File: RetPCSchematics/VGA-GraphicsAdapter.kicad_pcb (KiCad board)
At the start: 2 copper layers, 183.4 x 101.3 mm, 40 parts, among them J1 Bus_ISA_8bit, J2 74320-9004, U1 74AUC2G125, U10 ATmega644P-20PU, U11 628128, U12 628128, U13 SN74LVC245AN, U14 74LS245, U15 74LVC2G240, U16 74LVC2G240, U17 74LVC1G18, U18 74LVC1G18, U19 74LVC1G18, U2 74LVC2G240, U20 74LVC1G18, U21 ATF22V10D, U22 74LS245, U23 74LVC1G373, U24 74LVC1G373, U25 74LVC1G373, U26 74LVC1G373, U27 74LVC1G373, U28 74LVC1G373, U29 74LVC1G373, U3 ATF22V10D, U30 74LVC1G373, U31 74LVC1G373, U32 74LVC1G373, U33 74LVC1G373, U34 74LVC1G373, U36 TFP410, U37 ATF750C, U4 ATF22V10D, U5 74LS245, U6 ATF22V10D, U7 74LS245, U8 74LS245, U9 74LS245, X1 DGOF5S3

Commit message: EOD sync
Only control signals left to route
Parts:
- moved U2 108.6 mm to (157.1, 71.0), turned to 180 degrees
- moved U29 67.6 mm to (209.3, 76.2)
- moved U25 58.9 mm to (198.6, 56.0)
- moved U28 55.9 mm to (209.3, 72.4)
- moved U30 55.3 mm to (209.4, 64.3)
- moved U26 52.5 mm to (205.6, 48.6)
- moved U31 51.8 mm to (205.6, 57.1)
- moved U33 50.8 mm to (205.6, 52.6)
- moved U34 46.9 mm to (212.2, 52.5)
- moved U27 43.6 mm to (209.3, 68.7)
- moved U32 42.3 mm to (212.2, 48.3)
- moved X1 42.2 mm to (122.9, 57.4)
- moved U6 38.0 mm to (144.7, 57.9)
- moved U15 16.4 mm to (119.3, 106.8)
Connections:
- U2 pad 1: GND -> (no net)
- U2 pad 2: Net-(U2-Pad2) -> (no net)
- U2 pad 6: GEnd -> (no net)
- U4 pad 22: Net-(U2-Pad2) -> GEnd
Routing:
- net LoadEnable: track 0.00 -> 206.7 mm, vias 0 -> 9
- net GClock: track 0.00 -> 121.5 mm, vias 0 -> 5
- net DE: track 0.00 -> 79.4 mm
- net OP: track 0.00 -> 67.7 mm, vias 0 -> 3
- net Net-(U23-Pad4): track 0.00 -> 63.7 mm, vias 0 -> 3
- net Net-(U24-Pad4): track 0.00 -> 62.8 mm, vias 0 -> 2
- net Net-(U26-Pad4): track 0.00 -> 56.0 mm, vias 0 -> 5
- net Net-(U25-Pad4): track 0.00 -> 54.6 mm, vias 0 -> 4
- net Net-(U32-Pad4): track 0.00 -> 50.8 mm, vias 0 -> 2
- net Net-(U34-Pad4): track 0.00 -> 40.5 mm, vias 0 -> 4
- net Net-(U31-Pad4): track 0.00 -> 39.1 mm, vias 0 -> 2
- net Net-(U33-Pad4): track 0.00 -> 39.1 mm, vias 0 -> 1
- net Net-(U28-Pad4): track 0.00 -> 38.5 mm, vias 0 -> 3
- net Net-(U27-Pad4): track 0.00 -> 33.3 mm, vias 0 -> 2
- net Net-(U30-Pad4): track 0.00 -> 31.7 mm, vias 0 -> 2
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
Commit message: EOD sync
end of day sync
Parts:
- added REF**: PinHeader_1x02_P1.00mm_Vertical, Connector_PinHeader_1.00mm:PinHeader_1x02_P1.00mm_Vertical, F.Cu at (219.8, 48.0)
- moved J1 0.68 mm to (184.4, 135.3)
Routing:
- net Net-(U16-Pad3): track 0.00 -> 66.2 mm, vias 0 -> 3
- net GEnd: track 0.00 -> 55.3 mm, vias 0 -> 1
- net Net-(J2-Pad18): track 0.00 -> 28.7 mm, vias 0 -> 1
- net ALEN: track 27.3 -> 53.8 mm, vias 0 -> 3
- net Net-(J2-Pad23): track 0.00 -> 23.3 mm, vias 0 -> 1
- net Net-(J2-Pad17): track 0.00 -> 23.1 mm, vias 0 -> 1
- net GClock: track 121.5 -> 144.4 mm, vias 5 -> 6
- net Net-(J2-Pad24): track 0.00 -> 20.1 mm, vias 0 -> 1
- net Net-(J2-Pad9): track 0.00 -> 15.2 mm, vias 0 -> 1
- net Net-(J2-Pad1): track 0.00 -> 14.0 mm, vias 0 -> 1
- net Net-(J2-Pad2): track 0.00 -> 13.2 mm, vias 0 -> 1
- net /A0: track 1222.7 -> 1225.2 mm, vias 26 -> 28
- added copper zone on F.Cu, net GND
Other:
- board size 183.4 x 101.3 mm -> 136.7 x 101.3 mm

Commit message: sync
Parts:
- removed the REF** at (219.8, 48.0)
- added J3: Conn_01x02_Male, Connector_PinHeader_1.00mm:PinHeader_1x02_P1.00mm_Vertical, F.Cu at (218.2, 47.2)
- added REF**: OSHW-Symbol_6.7x6mm_SilkScreen, Symbol:OSHW-Symbol_6.7x6mm_SilkScreen, F.Cu at (232.5, 49.2)
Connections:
- U37 pad 14: Hsync -> Vsync
- U37 pad 15: Vsync -> Hsync
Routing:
- net RST: track 0.00 -> 131.1 mm, vias 0 -> 3
- net CS: track 30.4 -> 99.6 mm, vias 2 -> 8
- net GClock: track 144.4 -> 210.3 mm, vias 6 -> 8
- net CS(inv): track 0.00 -> 65.8 mm, vias 0 -> 3
- net +3V3: track 0.00 -> 60.4 mm, vias 0 -> 4
- net IOW: track 46.8 -> 105.1 mm, vias 1 -> 3
- net AEN: track 0.00 -> 57.4 mm
- net RST(inv): track 0.00 -> 54.8 mm, vias 0 -> 2
- net ALEN(inv): track 0.00 -> 48.0 mm, vias 0 -> 1
- net ALEN: track 53.8 -> 80.8 mm
- net Hsync: track 0.00 -> 26.0 mm
- net Vsync: track 0.00 -> 23.2 mm
- net Net-(J2-Pad10): track 0.00 -> 17.7 mm
- net LoadEnable: track 206.7 -> 191.4 mm
- net /A0: track 1225.2 -> 1222.6 mm
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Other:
- net class smol added: clearance 0.2, trace_width 0.1, via_dia 0.8, via_drill 0.4
- rule trace_min: 0.2 -> 0.1
- board text added: "CGA-DVI Adapter REV3.0"
- board text added: "M.Lind"
- board text added: "R.Doverfelt"
- board text added: "Unchecked Cast"

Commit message: EOD sync
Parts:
- added ?: , , F.Cu at (216.7, 101.6)
- added ?: , , F.Cu at (210.3, 76.2)
- added ?: , , F.Cu at (210.5, 76.1)
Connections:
- J1 pad 1: Net-(J1-Pad1) -> GND
- J1 pad 29: Net-(J1-Pad29) -> +5V
- J1 pad 31: Net-(J1-Pad31) -> GND
- U1 pad 8: VCC -> +5V
- U17 pad 5: VCC -> +3V3
- U18 pad 5: VCC -> +3V3
- U19 pad 5: VCC -> +3V3
- U20 pad 5: VCC -> +3V3
- U23 pad 5: VCC -> +3V3
- U24 pad 5: VCC -> +3V3
- U25 pad 5: VCC -> +3V3
- U26 pad 5: VCC -> +3V3
- U27 pad 5: VCC -> +3V3
- U28 pad 5: VCC -> +3V3
- U29 pad 5: VCC -> +3V3
- U30 pad 5: VCC -> +3V3
- U31 pad 5: VCC -> +3V3
- U32 pad 5: VCC -> +3V3
- U33 pad 5: VCC -> +3V3
- U34 pad 5: VCC -> +3V3
- U37 pad 24: +5V -> +3V3
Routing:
- net GND: track 31.8 -> 262.6 mm, vias 0 -> 18
- net +3V3: track 60.4 -> 142.5 mm, vias 4 -> 13
- net +5V: track 0.00 -> 39.0 mm, vias 0 -> 6
- net LoadEnable: track 191.4 -> 229.6 mm, vias 9 -> 10
- net DR: track 0.00 -> 37.6 mm, vias 0 -> 1
- net Net-(U16-Pad3): track 66.2 -> 97.4 mm, vias 3 -> 10
- net VCC: track 0.00 -> 20.1 mm, vias 0 -> 5
- net Net-(RN1-Pad4): track 2.79 -> 20.2 mm, vias 0 -> 4
- net Net-(RN1-Pad3): track 2.79 -> 20.2 mm, vias 0 -> 3
- net Net-(RN1-Pad5): track 2.79 -> 17.7 mm, vias 0 -> 2
- net Net-(U10-Pad21): track 47.4 -> 61.2 mm
- net Net-(RN1-Pad2): track 2.79 -> 8.48 mm, vias 0 -> 2
- net Net-(U24-Pad4): track 62.8 -> 65.5 mm
- net Net-(U25-Pad4): track 54.6 -> 57.1 mm
- net Net-(U20-Pad6): track 16.5 -> 18.1 mm
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- added copper zone on B.Cu, net +3V3
- added copper zone on B.Cu, net +5V
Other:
- net class smol: via_dia 0.8 -> 0.6
- rule via_min_size: 0.4 -> 0.6

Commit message: Some relabeling and cleanup of CGA-card
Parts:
- removed ? (x3): , 
- removed REF**: OSHW-Symbol_6.7x6mm_SilkScreen, Symbol:OSHW-Symbol_6.7x6mm_SilkScreen
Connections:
- J1 pad 10: Net-(J1-Pad10) -> (no net)
- J1 pad 11: Net-(J1-Pad11) -> (no net)
- J1 pad 12: Net-(J1-Pad12) -> (no net)
- J1 pad 14: Net-(J1-Pad14) -> (no net)
- J1 pad 15: Net-(J1-Pad15) -> (no net)
- J1 pad 16: Net-(J1-Pad16) -> (no net)
- J1 pad 17: Net-(J1-Pad17) -> (no net)
- J1 pad 18: Net-(J1-Pad18) -> (no net)
- J1 pad 19: Net-(J1-Pad19) -> (no net)
- J1 pad 20: Net-(J1-Pad20) -> (no net)
- J1 pad 21: Net-(J1-Pad21) -> (no net)
- J1 pad 22: Net-(J1-Pad22) -> (no net)
- J1 pad 23: Net-(J1-Pad23) -> (no net)
- J1 pad 24: Net-(J1-Pad24) -> (no net)
- J1 pad 25: Net-(J1-Pad25) -> (no net)
- J1 pad 26: Net-(J1-Pad26) -> (no net)
- J1 pad 27: Net-(J1-Pad27) -> (no net)
- J1 pad 29: +5V -> +3V3
- J1 pad 3: Net-(J1-Pad3) -> +3V3
- J1 pad 30: Net-(J1-Pad30) -> (no net)
- J1 pad 32: Net-(J1-Pad32) -> (no net)
- J1 pad 4: Net-(J1-Pad4) -> (no net)
- J1 pad 41: Net-(J1-Pad41) -> (no net)
- J1 pad 5: Net-(J1-Pad5) -> (no net)
- J1 pad 58: /A0 -> /A4
- J1 pad 59: /A0 -> /A3
- J1 pad 6: Net-(J1-Pad6) -> (no net)
- J1 pad 60: /A0 -> /A2
- J1 pad 61: /A0 -> /A1
- J1 pad 7: Net-(J1-Pad7) -> (no net)
- J1 pad 8: Net-(J1-Pad8) -> (no net)
- J1 pad 9: Net-(J1-Pad9) -> (no net)
- J2 pad 14: +5V -> +3V3
- U1 pad 2: /A16 -> /XA16
- U1 pad 3: /A17 -> (no net)
- U1 pad 5: /A17 -> /XA17
- U1 pad 6: /A16 -> /VA16
- U1 pad 8: +5V -> +3V3
- U10 pad 1: /A9 -> /XA9
- U10 pad 10: +5V -> +3V3
- U10 pad 12: Net-(U10-Pad12) -> (no net)
- U10 pad 13: Net-(U10-Pad13) -> (no net)
- U10 pad 2: /A8 -> /XA8
- U10 pad 22: /A0 -> /XA1
- U10 pad 23: /A0 -> /XA0
- U10 pad 27: CountReset -> (no net)
- U10 pad 3: /A7 -> /XA7
- U10 pad 30: Net-(U10-Pad30) -> +3V3
- U10 pad 33: /A17 -> /XA17
- U10 pad 34: /A16 -> /XA16
- U10 pad 35: /A15 -> /XA15
- U10 pad 36: /A14 -> /XA14
- U10 pad 37: /A13 -> /XA13
- U10 pad 38: /A12 -> /XA12
- U10 pad 39: /A11 -> /XA11
- U10 pad 4: /A6 -> /XA6
- U10 pad 40: /A10 -> /XA10
- U10 pad 5: /A5 -> /XA5
- U10 pad 6: /A0 -> /XA4
- U10 pad 7: /A0 -> /XA3
- U10 pad 8: /A0 -> /XA2
- U11 pad 10: /A0 -> /VA2
- U11 pad 11: /A0 -> /VA1
- U11 pad 12: /A0 -> /VA0
- U11 pad 2: /A16 -> /VA16
- U11 pad 23: /A10 -> /VA10
- U11 pad 25: /A11 -> /VA11
- U11 pad 26: /A9 -> /VA9
- U11 pad 27: /A8 -> /VA8
- U11 pad 28: /A13 -> /VA13
- U11 pad 3: /A14 -> /VA14
- U11 pad 31: /A15 -> /VA15
- U11 pad 32: VCC -> +3V3
- U11 pad 4: /A12 -> /VA12
- U11 pad 5: /A7 -> /VA7
- U11 pad 6: /A6 -> /VA6
- U11 pad 7: /A5 -> /VA5
- U11 pad 8: /A0 -> /VA4
- U11 pad 9: /A0 -> /VA3
- U12 pad 10: /A0 -> /VA2
- U12 pad 11: /A0 -> /VA1
- U12 pad 12: /A0 -> /VA0
- U12 pad 2: /A16 -> /VA16
- U12 pad 23: /A10 -> /VA10
- U12 pad 25: /A11 -> /VA11
- U12 pad 26: /A9 -> /VA9
- U12 pad 27: /A8 -> /VA8
- U12 pad 28: /A13 -> /VA13
- U12 pad 3: /A14 -> /VA14
- U12 pad 31: /A15 -> /VA15
- U12 pad 32: VCC -> +3V3
- U12 pad 4: /A12 -> /VA12
- U12 pad 5: /A7 -> /VA7
- U12 pad 6: /A6 -> /VA6
- U12 pad 7: /A5 -> /VA5
- U12 pad 8: /A0 -> /VA4
- U12 pad 9: /A0 -> /VA3
- U14 pad 20: +5V -> +3V3
- U15 pad 8: VCC -> +3V3
- U16 pad 6: (inv)LE -> (no net)
- U16 pad 8: VCC -> +3V3
- U2 pad 8: VCC -> +3V3
- U21 pad 14: /A0 -> /A1
- U21 pad 15: /A0 -> /A2
- U21 pad 16: /A0 -> /A3
- U21 pad 17: /A0 -> /A4
- U21 pad 24: +5V -> +3V3
- U22 pad 20: +5V -> +3V3
- U29 pad 6: Net-(U29-Pad6) -> (no net)
- U3 pad 10: Net-(U3-Pad10) -> (no net)
- U3 pad 11: Net-(U3-Pad11) -> (no net)
- U3 pad 13: Net-(U3-Pad13) -> (no net)
- U3 pad 14: /A0 -> /VA0
- U3 pad 15: /A0 -> /VA1
- U3 pad 16: /A0 -> /VA2
- U3 pad 17: /A0 -> /VA3
- U3 pad 18: /A0 -> /VA4
- U3 pad 19: /A5 -> /VA5
- U3 pad 2: Net-(U3-Pad2) -> (no net)
- U3 pad 20: /A6 -> /VA6
- U3 pad 21: /A7 -> /VA7
- U3 pad 22: /A8 -> /VA8
- U3 pad 23: /A9 -> /VA9
- U3 pad 24: +5V -> +3V3
- U3 pad 3: Net-(U3-Pad3) -> (no net)
- U3 pad 4: Net-(U3-Pad4) -> (no net)
- U3 pad 5: Net-(U3-Pad5) -> (no net)
- U3 pad 6: Net-(U3-Pad6) -> (no net)
- U3 pad 7: Net-(U3-Pad7) -> (no net)
- U3 pad 8: Net-(U3-Pad8) -> (no net)
- U3 pad 9: Net-(U3-Pad9) -> (no net)
- U36 pad 11: Net-(U36-Pad11) -> (no net)
- U36 pad 19: Net-(U36-Pad19) -> (no net)
- U36 pad 49: Net-(U36-Pad49) -> (no net)
- U36 pad 65: Net-(U36-Pad65) -> GND
- U37 pad 10: Net-(U37-Pad10) -> (no net)
- U37 pad 11: Net-(U37-Pad11) -> (no net)
- U37 pad 13: Net-(U37-Pad13) -> (no net)
- U37 pad 16: Net-(U37-Pad16) -> (no net)
- U37 pad 17: Net-(U37-Pad17) -> (no net)
- U37 pad 18: Net-(U37-Pad18) -> (no net)
- U37 pad 19: Net-(U37-Pad19) -> (no net)
- U37 pad 20: Net-(U37-Pad20) -> (no net)
- U37 pad 21: Net-(U37-Pad21) -> (no net)
- U37 pad 22: Net-(U37-Pad22) -> (no net)
- U37 pad 4: Net-(U37-Pad4) -> (no net)
- U37 pad 5: Net-(U37-Pad5) -> (no net)
- U37 pad 6: Net-(U37-Pad6) -> (no net)
- U37 pad 7: Net-(U37-Pad7) -> (no net)
- U37 pad 8: Net-(U37-Pad8) -> (no net)
- U37 pad 9: Net-(U37-Pad9) -> (no net)
- U4 pad 1: /A9 -> /VA9
- U4 pad 10: /A0 -> /VA0
- U4 pad 11: Net-(U4-Pad11) -> (no net)
- U4 pad 13: Net-(U4-Pad13) -> (no net)
- U4 pad 14: /A10 -> /VA10
- U4 pad 15: /A11 -> /VA11
- U4 pad 16: /A12 -> /VA12
- U4 pad 17: /A13 -> /VA13
- U4 pad 18: /A14 -> /VA14
- U4 pad 19: /A15 -> /VA15
- U4 pad 2: /A8 -> /VA8
- U4 pad 20: /A16 -> /VA16
- U4 pad 23: Net-(U4-Pad23) -> (no net)
- U4 pad 24: +5V -> +3V3
- U4 pad 3: /A7 -> /VA7
- U4 pad 4: /A6 -> /VA6
- U4 pad 5: /A5 -> /VA5
- U4 pad 6: /A0 -> /VA4
- U4 pad 7: /A0 -> /VA3
- U4 pad 8: /A0 -> /VA2
- U4 pad 9: /A0 -> /VA1
- U5 pad 11: /A15 -> /VA15
- U5 pad 12: /A14 -> /VA14
- U5 pad 13: /A13 -> /VA13
- U5 pad 14: /A12 -> /VA12
- U5 pad 15: /A11 -> /VA11
- U5 pad 16: /A10 -> /VA10
- U5 pad 17: /A9 -> /VA9
- U5 pad 18: /A8 -> /VA8
- U5 pad 2: /A8 -> /XA8
- U5 pad 20: +5V -> +3V3
- U5 pad 3: /A9 -> /XA9
- U5 pad 4: /A10 -> /XA10
- U5 pad 5: /A11 -> /XA11
- U5 pad 6: /A12 -> /XA12
- U5 pad 7: /A13 -> /XA13
- U5 pad 8: /A14 -> /XA14
- U5 pad 9: /A15 -> /XA15
- U6 pad 10: Net-(U6-Pad10) -> (no net)
- U6 pad 11: Net-(U6-Pad11) -> (no net)
- U6 pad 12: Net-(U6-Pad12) -> GND
- U6 pad 13: Net-(U6-Pad13) -> (no net)
- U6 pad 17: Net-(U6-Pad17) -> (no net)
- U6 pad 18: Net-(U6-Pad18) -> (no net)
- U6 pad 19: Net-(U6-Pad19) -> (no net)
- U6 pad 20: Net-(U6-Pad20) -> (no net)
- U6 pad 21: Net-(U6-Pad21) -> (no net)
- U6 pad 22: Net-(U6-Pad22) -> (no net)
- U6 pad 23: Net-(U6-Pad23) -> (no net)
- U6 pad 24: Net-(U6-Pad24) -> +3V3
- U6 pad 3: Net-(U6-Pad3) -> (no net)
- U6 pad 4: Net-(U6-Pad4) -> (no net)
- U6 pad 5: Net-(U6-Pad5) -> (no net)
- U6 pad 6: Net-(U6-Pad6) -> (no net)
- U6 pad 7: Net-(U6-Pad7) -> (no net)
- U6 pad 8: Net-(U6-Pad8) -> (no net)
- U6 pad 9: Net-(U6-Pad9) -> (no net)
- U7 pad 11: /A15 -> /XA15
- U7 pad 12: /A14 -> /XA14
- U7 pad 13: /A13 -> /XA13
- U7 pad 14: /A12 -> /XA12
- U7 pad 15: /A11 -> /XA11
- U7 pad 16: /A10 -> /XA10
- U7 pad 17: /A9 -> /XA9
- U7 pad 18: /A8 -> /XA8
- U7 pad 20: +5V -> +3V3
- U8 pad 11: /A7 -> /VA7
- U8 pad 12: /A6 -> /VA6
- U8 pad 13: /A5 -> /VA5
- U8 pad 14: /A0 -> /VA4
- U8 pad 15: /A0 -> /VA3
- U8 pad 16: /A0 -> /VA2
- U8 pad 17: /A0 -> /VA1
- U8 pad 18: /A0 -> /VA0
- U8 pad 2: /A0 -> /XA0
- U8 pad 20: +5V -> +3V3
- U8 pad 3: /A0 -> /XA1
- U8 pad 4: /A0 -> /XA2
- U8 pad 5: /A0 -> /XA3
- U8 pad 6: /A0 -> /XA4
- U8 pad 7: /A5 -> /XA5
- U8 pad 8: /A6 -> /XA6
- U8 pad 9: /A7 -> /XA7
- U9 pad 11: /A7 -> /XA7
- U9 pad 12: /A6 -> /XA6
- U9 pad 13: /A5 -> /XA5
- U9 pad 14: /A0 -> /XA4
- U9 pad 15: /A0 -> /XA3
- U9 pad 16: /A0 -> /XA2
- U9 pad 17: /A0 -> /XA1
- U9 pad 18: /A0 -> /XA0
- U9 pad 20: +5V -> +3V3
- U9 pad 3: /A0 -> /A1
- U9 pad 4: /A0 -> /A2
- U9 pad 5: /A0 -> /A3
- U9 pad 6: /A0 -> /A4
- X1 pad 1: Net-(X1-Pad1) -> (no net)
- X1 pad 14: +5V -> +3V3
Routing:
- net /A0: track 1223.5 -> 73.5 mm, vias 28 -> 2
- net /A5: track 204.2 -> 60.8 mm, vias 5 -> 1
- net /A6: track 196.7 -> 64.5 mm, vias 6 -> 1
- net /A15: track 171.6 -> 45.7 mm, vias 1 -> 0
- net /A13: track 171.5 -> 45.9 mm, vias 3 -> 0
- net /A11: track 170.5 -> 45.9 mm, vias 8 -> 0
- net /A7: track 179.6 -> 60.2 mm, vias 5 -> 1
- net /VA0: track 0.00 -> 116.2 mm, vias 0 -> 4
- net /A10: track 158.4 -> 45.9 mm, vias 2 -> 0
- net /VA1: track 0.00 -> 110.7 mm, vias 0 -> 4
- net /A12: track 155.5 -> 45.9 mm, vias 5 -> 0
- net /VA2: track 0.00 -> 109.3 mm, vias 0 -> 4
- net /VA5: track 0.00 -> 108.0 mm, vias 0 -> 4
- net /VA3: track 0.00 -> 107.4 mm, vias 0 -> 4
- net /VA4: track 0.00 -> 105.6 mm, vias 0 -> 4
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
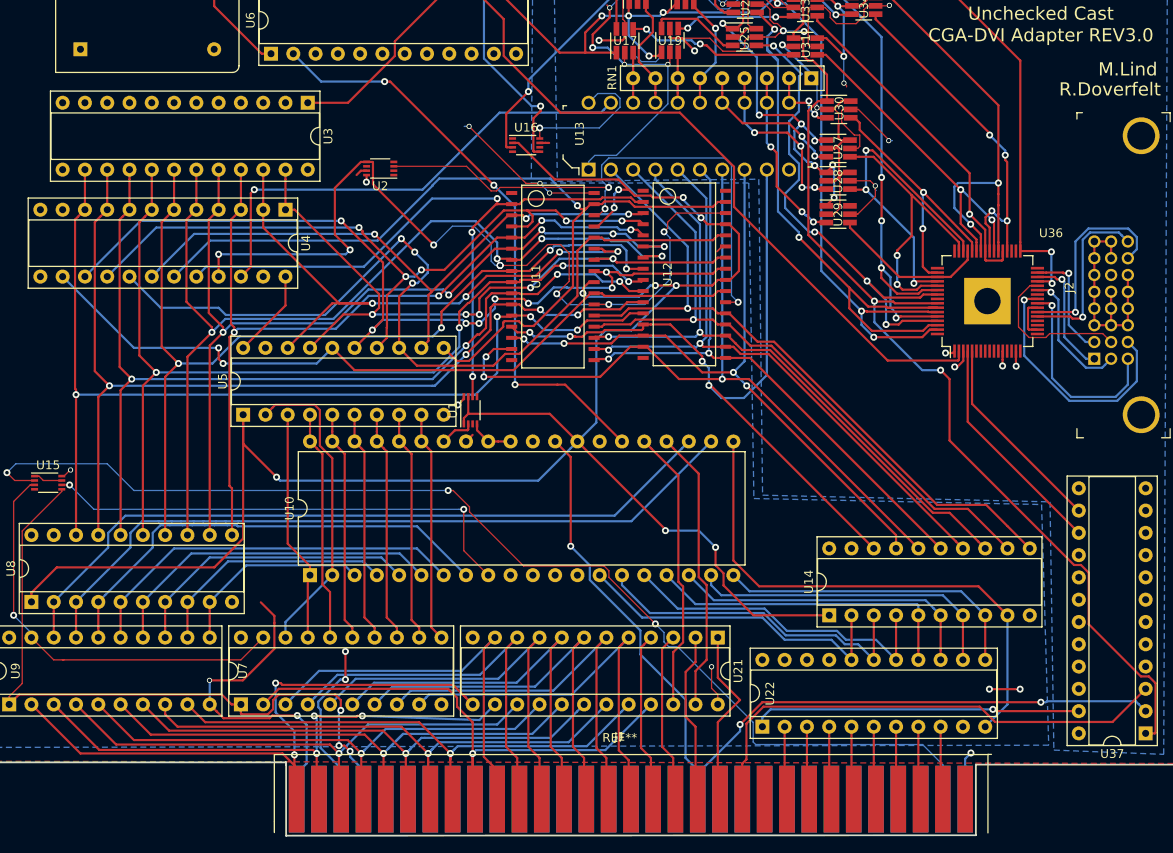
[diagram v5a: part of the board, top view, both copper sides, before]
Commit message: Ready made the design for graphics card
Routed the final pads. DO NOT CHANGE THE NETLIST!!!
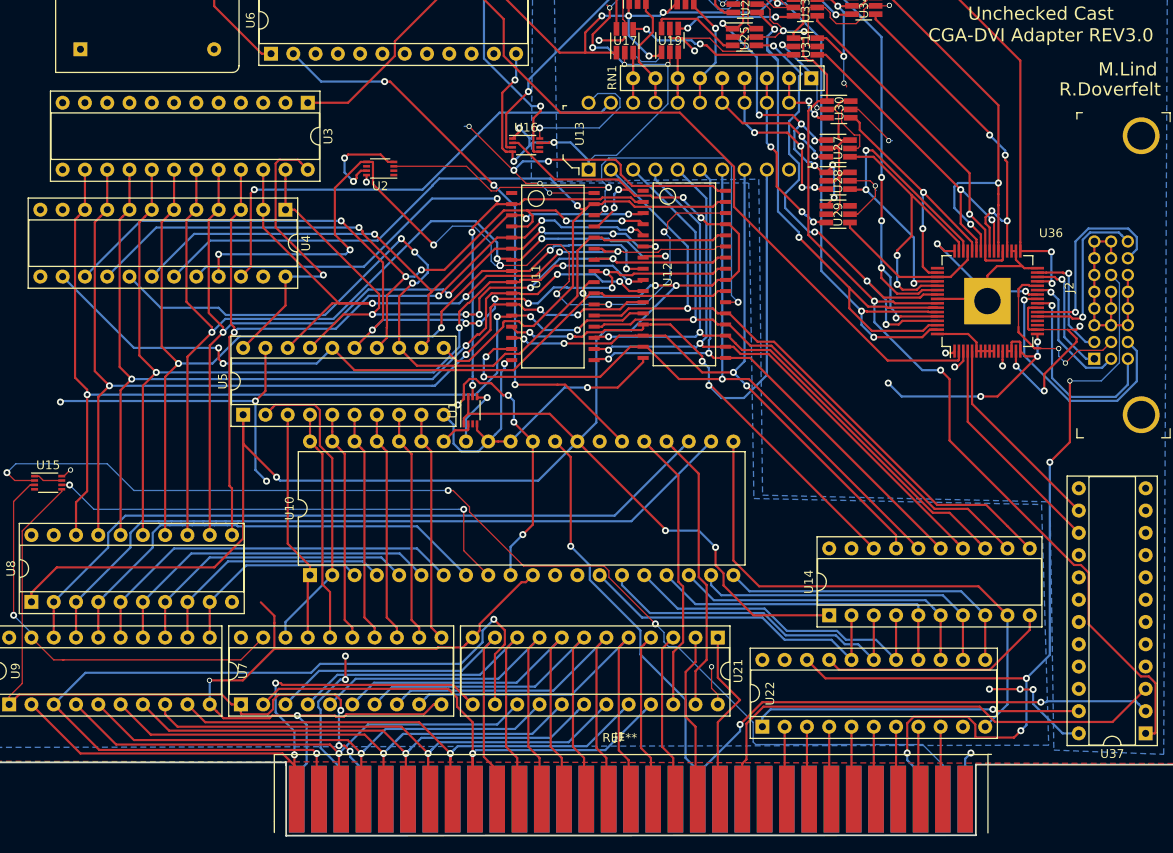
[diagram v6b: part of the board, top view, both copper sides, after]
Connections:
- J1 pad 10: (no net) -> Net-(J1-Pad10)
- J1 pad 11: (no net) -> Net-(J1-Pad11)
- J1 pad 12: (no net) -> Net-(J1-Pad12)
- J1 pad 14: (no net) -> Net-(J1-Pad14)
- J1 pad 15: (no net) -> Net-(J1-Pad15)
- J1 pad 16: (no net) -> Net-(J1-Pad16)
- J1 pad 17: (no net) -> Net-(J1-Pad17)
- J1 pad 18: (no net) -> Net-(J1-Pad18)
- J1 pad 19: (no net) -> Net-(J1-Pad19)
- J1 pad 20: (no net) -> Net-(J1-Pad20)
- J1 pad 21: (no net) -> Net-(J1-Pad21)
- J1 pad 22: (no net) -> Net-(J1-Pad22)
- J1 pad 23: (no net) -> Net-(J1-Pad23)
- J1 pad 24: (no net) -> Net-(J1-Pad24)
- J1 pad 25: (no net) -> Net-(J1-Pad25)
- J1 pad 26: (no net) -> Net-(J1-Pad26)
- J1 pad 27: (no net) -> Net-(J1-Pad27)
- J1 pad 29: +3V3 -> +5V
- J1 pad 3: +3V3 -> +5V
- J1 pad 30: (no net) -> Net-(J1-Pad30)
- J1 pad 32: (no net) -> Net-(J1-Pad32)
- J1 pad 4: (no net) -> Net-(J1-Pad4)
- J1 pad 41: (no net) -> Net-(J1-Pad41)
- J1 pad 5: (no net) -> Net-(J1-Pad5)
- J1 pad 6: (no net) -> Net-(J1-Pad6)
- J1 pad 7: (no net) -> Net-(J1-Pad7)
- J1 pad 8: (no net) -> Net-(J1-Pad8)
- J1 pad 9: (no net) -> Net-(J1-Pad9)
- J2 pad 14: +3V3 -> +5V
- U1 pad 3: (no net) -> /VA17
- U1 pad 8: +3V3 -> +5V
- U10 pad 10: +3V3 -> +5V
- U10 pad 12: (no net) -> Net-(U10-Pad12)
- U10 pad 13: (no net) -> Net-(U10-Pad13)
- U10 pad 27: (no net) -> CountReset
- U10 pad 30: +3V3 -> +5V
- U11 pad 32: +3V3 -> +5V
- U12 pad 32: +3V3 -> +5V
- U14 pad 20: +3V3 -> +5V
- U15 pad 8: +3V3 -> +5V
- U16 pad 6: (no net) -> (inv)LE
- U2 pad 8: +3V3 -> +5V
- U21 pad 24: +3V3 -> +5V
- U22 pad 20: +3V3 -> +5V
- U29 pad 6: (no net) -> Net-(U29-Pad6)
- U3 pad 10: (no net) -> Net-(U3-Pad10)
- U3 pad 11: (no net) -> Net-(U3-Pad11)
- U3 pad 13: (no net) -> Net-(U3-Pad13)
- U3 pad 2: (no net) -> Net-(U3-Pad2)
- U3 pad 24: +3V3 -> +5V
- U3 pad 3: (no net) -> Net-(U3-Pad3)
- U3 pad 4: (no net) -> Net-(U3-Pad4)
- U3 pad 5: (no net) -> Net-(U3-Pad5)
- U3 pad 6: (no net) -> Net-(U3-Pad6)
- U3 pad 7: (no net) -> Net-(U3-Pad7)
- U3 pad 8: (no net) -> Net-(U3-Pad8)
- U3 pad 9: (no net) -> Net-(U3-Pad9)
- U36 pad 11: (no net) -> Net-(U36-Pad11)
- U36 pad 19: (no net) -> Net-(U36-Pad19)
- U36 pad 49: (no net) -> Net-(U36-Pad49)
- U37 pad 10: (no net) -> Net-(U37-Pad10)
- U37 pad 11: (no net) -> Net-(U37-Pad11)
- U37 pad 13: (no net) -> Net-(U37-Pad13)
- U37 pad 16: (no net) -> Net-(U37-Pad16)
- U37 pad 17: (no net) -> Net-(U37-Pad17)
- U37 pad 18: (no net) -> Net-(U37-Pad18)
- U37 pad 19: (no net) -> Net-(U37-Pad19)
- U37 pad 20: (no net) -> Net-(U37-Pad20)
- U37 pad 21: (no net) -> Net-(U37-Pad21)
- U37 pad 22: (no net) -> Net-(U37-Pad22)
- U37 pad 4: (no net) -> Net-(U37-Pad4)
- U37 pad 5: (no net) -> Net-(U37-Pad5)
- U37 pad 6: (no net) -> Net-(U37-Pad6)
- U37 pad 7: (no net) -> Net-(U37-Pad7)
- U37 pad 8: (no net) -> Net-(U37-Pad8)
- U37 pad 9: (no net) -> Net-(U37-Pad9)
- U4 pad 11: (no net) -> Net-(U4-Pad11)
- U4 pad 13: (no net) -> Net-(U4-Pad13)
- U4 pad 23: (no net) -> Net-(U4-Pad23)
- U4 pad 24: +3V3 -> +5V
- U5 pad 20: +3V3 -> +5V
- U6 pad 10: (no net) -> Net-(U6-Pad10)
- U6 pad 11: (no net) -> Net-(U6-Pad11)
- U6 pad 13: (no net) -> Net-(U6-Pad13)
- U6 pad 17: (no net) -> Net-(U6-Pad17)
- U6 pad 18: (no net) -> Net-(U6-Pad18)
- U6 pad 19: (no net) -> Net-(U6-Pad19)
- U6 pad 20: (no net) -> Net-(U6-Pad20)
- U6 pad 21: (no net) -> Net-(U6-Pad21)
- U6 pad 22: (no net) -> Net-(U6-Pad22)
- U6 pad 23: (no net) -> Net-(U6-Pad23)
- U6 pad 24: +3V3 -> +5V
- U6 pad 3: (no net) -> Net-(U6-Pad3)
- U6 pad 4: (no net) -> Net-(U6-Pad4)
- U6 pad 5: (no net) -> Net-(U6-Pad5)
- U6 pad 6: (no net) -> Net-(U6-Pad6)
- U6 pad 7: (no net) -> Net-(U6-Pad7)
- U6 pad 8: (no net) -> Net-(U6-Pad8)
- U6 pad 9: (no net) -> Net-(U6-Pad9)
- U7 pad 20: +3V3 -> +5V
- U8 pad 20: +3V3 -> +5V
- U9 pad 20: +3V3 -> +5V
- X1 pad 1: (no net) -> Net-(X1-Pad1)
- X1 pad 14: +3V3 -> +5V
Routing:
- net GND: track 262.8 -> 527.8 mm, vias 19 -> 36
- net +5V: track 0.00 -> 245.3 mm, vias 0 -> 20
- net /A1: track 62.8 -> 102.5 mm, vias 3 -> 2
- net +3V3: track 234.9 -> 207.4 mm, vias 29 -> 23
- net /VA8: track 69.1 -> 80.9 mm
- net /XA17: track 1.07 -> 7.20 mm, vias 0 -> 1
- net Net-(J2-Pad10): track 17.7 -> 21.3 mm, vias 0 -> 2
- net /VA6: track 102.3 -> 100.3 mm
- net /VA5: track 108.0 -> 108.6 mm
